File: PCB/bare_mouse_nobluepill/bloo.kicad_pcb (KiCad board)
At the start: 4 copper layers, 84.9 x 94.9 mm, 111 parts, among them J1 Serial Debug Header, J10 Conn_01x06_Female, J2 SWD Header, J4 Conn_ARM_JTAG_SWD_10, M1 M1_Conn_Alt, M2 M2_Conn_Alt, Q0 Q_Photo_NPN, Q1 Q_Photo_NPN, Q10 Q_NMOS_GSD, Q11 Q_NMOS_GSD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

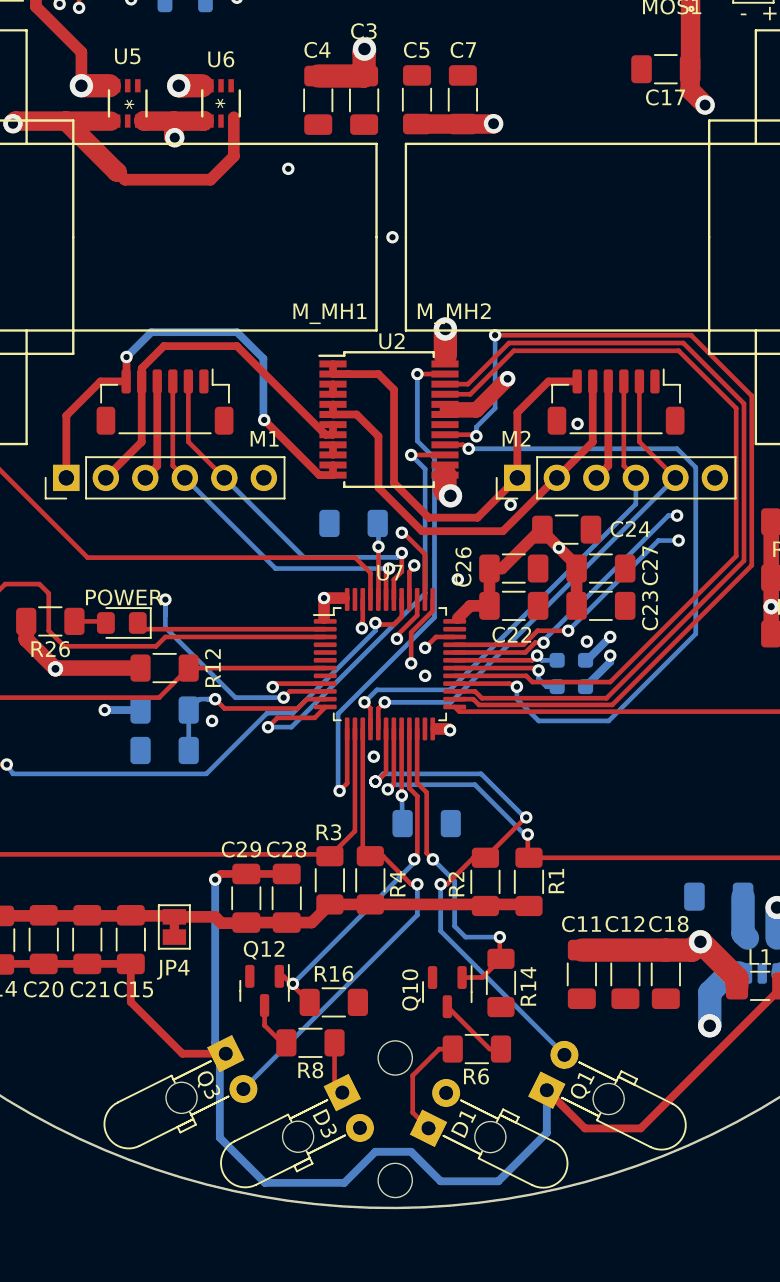
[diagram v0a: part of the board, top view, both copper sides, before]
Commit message: Fixed packet alignment for 24 byte packets.
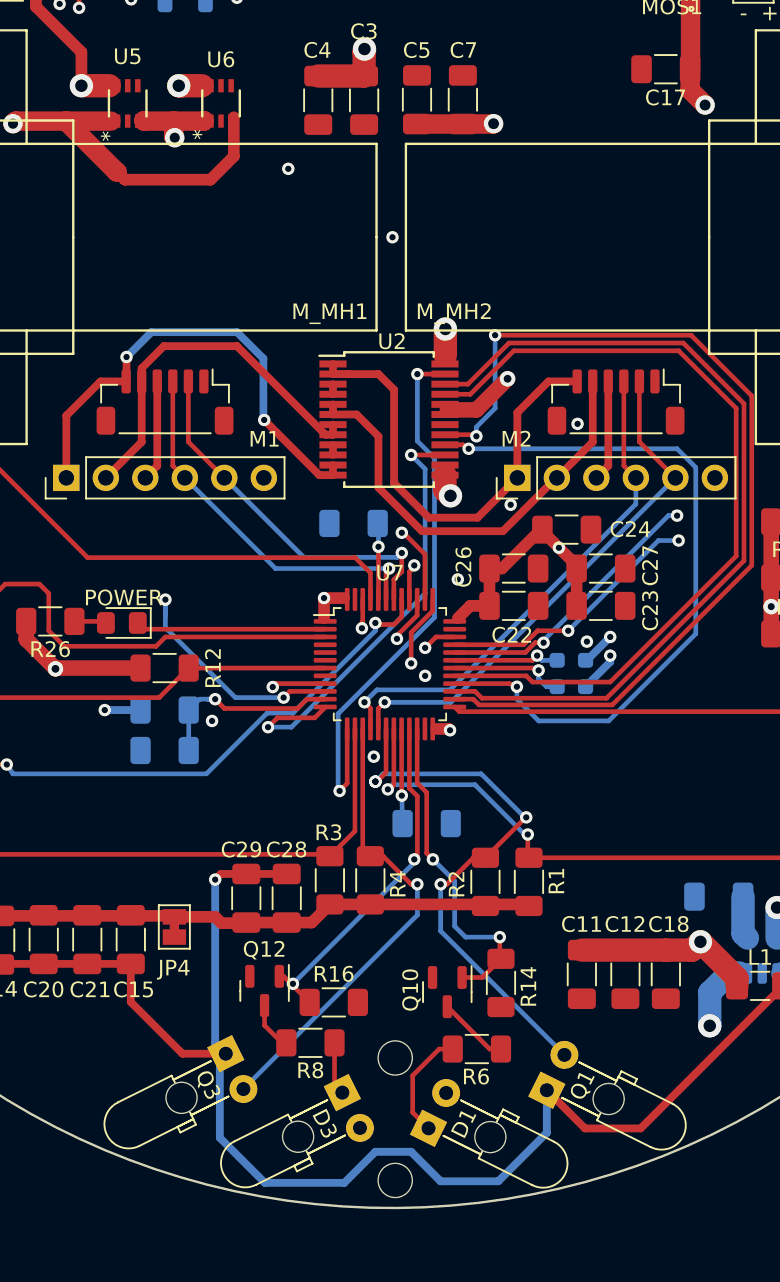
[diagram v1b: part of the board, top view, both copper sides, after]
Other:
- board text removed: "J. Low, T. Tang N. Ward v0.4 2024"
